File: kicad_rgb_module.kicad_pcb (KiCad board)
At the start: 2 copper layers, 25 x 25 mm, 42 parts, among them J1 Conn_HackConnect, SW1 TS-1088-AR02016, U1 STM32G030F6P6, U2 NCP114ASN330T1G

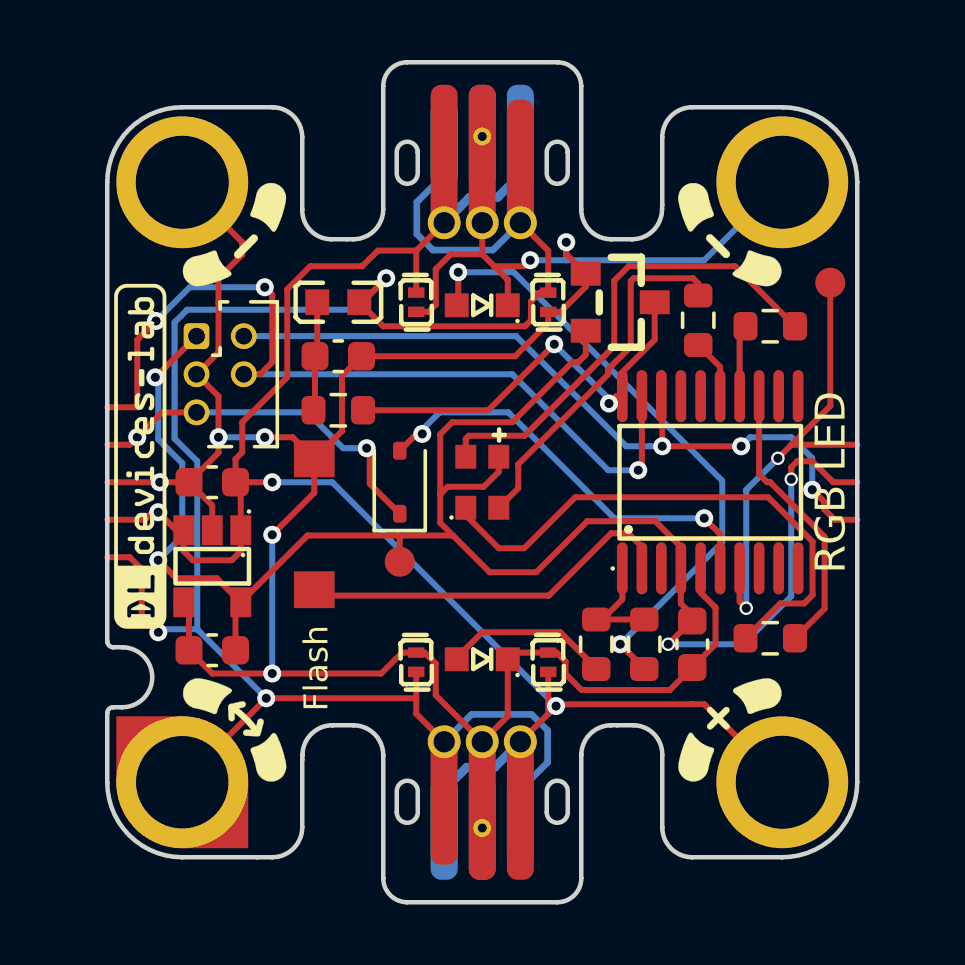
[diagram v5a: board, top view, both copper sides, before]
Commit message: Add final order DL-21-v0.1 gerbers (with BAT54S->BAS40-04 change, but only in BOM and CPL csvs, not kicad). Fix too small via pads, DNP C1, revert mounting hole soldermask back to normal.
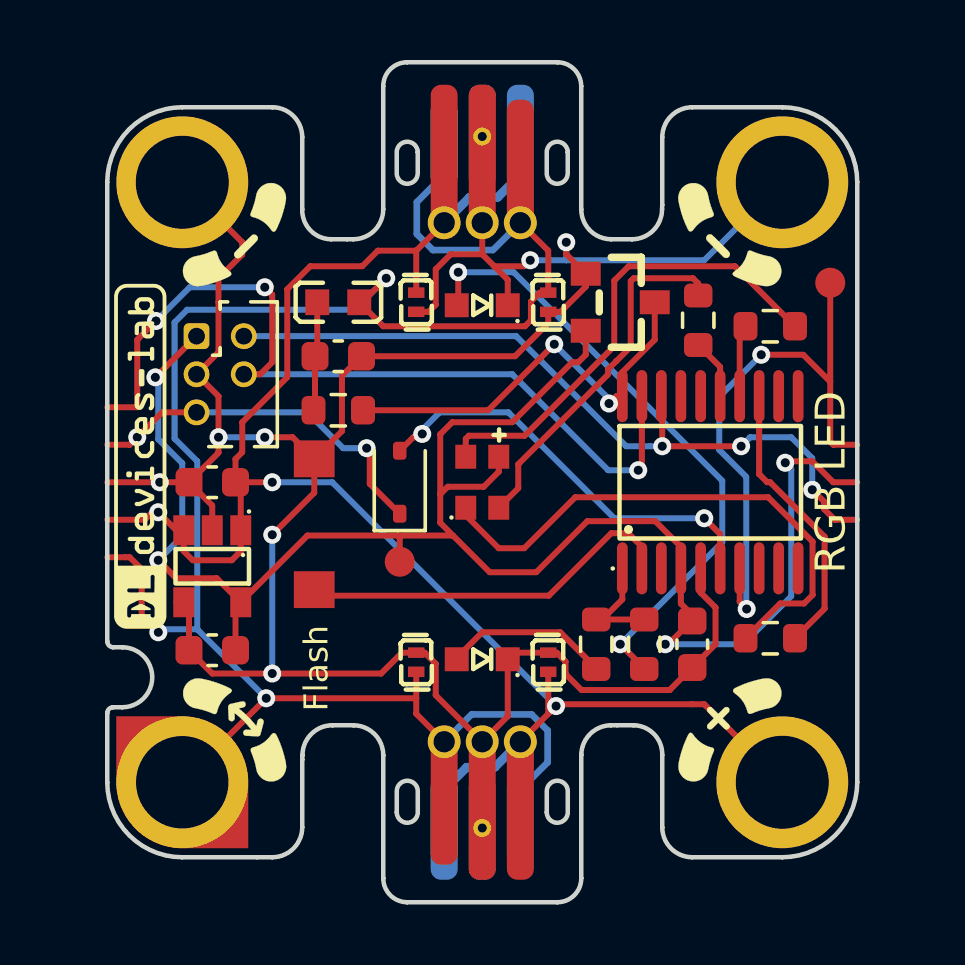
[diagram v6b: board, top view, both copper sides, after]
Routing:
- net /SERIAL: track 15.6 -> 19.8 mm
- net +3V3: track 60.2 -> 61.0 mm
